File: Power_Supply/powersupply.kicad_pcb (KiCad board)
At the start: 2 copper layers, 60.8 x 63.3 mm, 80 parts, among them J1 1x2, J101 USB_B_Micro, J102 Conn_01x03_Male, J103 Default_Jumper, J104 Default_Jumper, J2 1x2, Q1 IRF9Z24NPBF, SW1 KMR2, SW2 joystick-K1-1506DN-01, U101 AZ1117E-3.3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

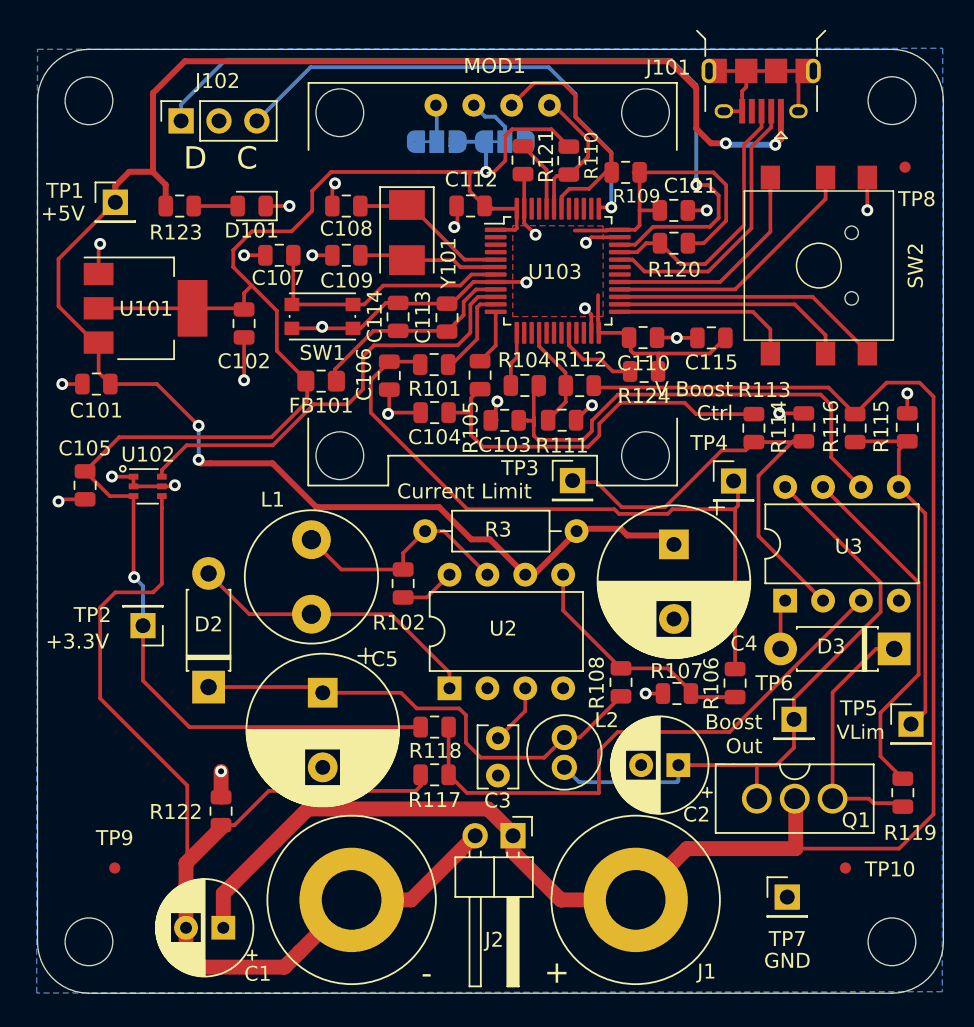
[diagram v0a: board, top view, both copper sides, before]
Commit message: Stuff for bootloader and MOSFET flat orientation
Moved power stuff to left and changed mosfet to flat orientation
Added LED for bootloader
Added button for entering bootloader mode
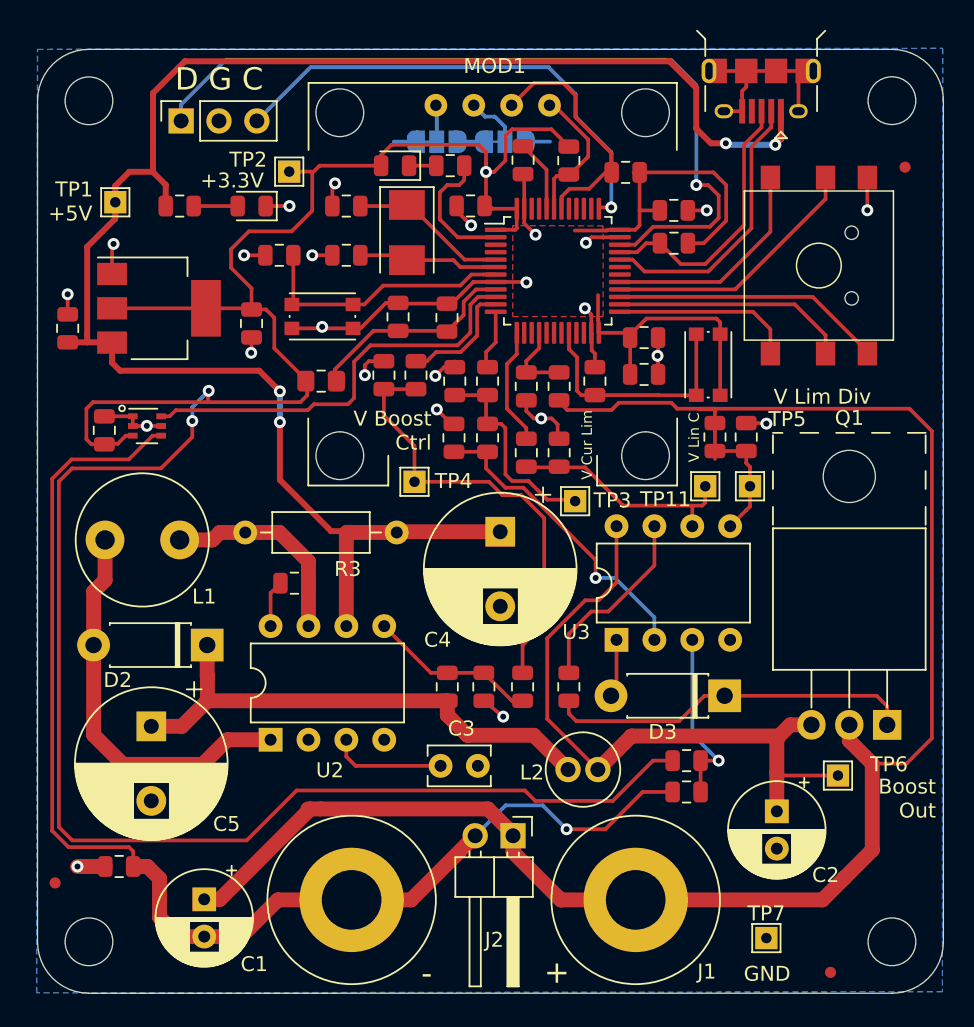
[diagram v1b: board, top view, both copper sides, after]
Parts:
- added D102: C503B 2.1V, LED_SMD:LED_0805_2012Metric, F.Cu at (52.8, 35.9)
- added G***: LOGO, powersupply:Logo, B.Cu at (60.1, 49.0)
- added R125: 4.99k, Resistor_SMD:R_0805_2012Metric, F.Cu at (56.5, 35.9)
- added SW3: KMR2, Button_Switch_SMD:SW_Push_1P1T_NO_CK_KMR2, F.Cu at (73.8, 49.2)
- added TP11: V_lin_ctrl, TestPoint:TestPoint_THTPad_1.5x1.5mm_Drill0.7mm, F.Cu at (73.6, 57.4)
- Q1: footprint powersupply:IRF9540N-PMOS -> Package_TO_SOT_THT:TO-220-3_Horizontal_TabUp
- R124: value 1.5k -> 4.99k
- TP1: value +5_isolated -> +5; footprint Connector_PinHeader_2.54mm:PinHeader_1x01_P2.54mm_Vertical -> TestPoint:TestPoint_THTPad_1.5x1.5mm_Drill0.7mm
- TP2, TP3, TP4, TP5, TP6, TP7: footprint Connector_PinHeader_2.54mm:PinHeader_1x01_P2.54mm_Vertical -> TestPoint:TestPoint_THTPad_1.5x1.5mm_Drill0.7mm
- moved TP2 32.0 mm to (45.7, 36.3)
- moved R119 23.5 mm to (64.5, 70.8)
- moved R114 23.5 mm to (56.8, 54.1)
- moved TP4 21.4 mm to (54.1, 57.1)
- moved TP5 19.3 mm to (76.6, 57.4)
- moved R113 17.9 mm to (59.0, 54.1)
- moved R118 17.0 mm to (72.3, 75.8)
- moved R117 16.9 mm to (72.3, 77.9)
- moved R106 14.3 mm to (61.4, 70.8)
- moved R107 13.0 mm to (58.8, 70.8), turned to 270 degrees
- moved U2 12.5 mm to (44.5, 74.4)
- moved R3 12.1 mm to (42.8, 60.5)
- moved D3 11.8 mm to (74.9, 71.5)
- moved C5 11.7 mm to (36.5, 73.5)
- moved C4 11.7 mm to (59.9, 60.5)
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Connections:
- R124 pad 1: +3V3 -> GND
- TP3 pad 1: /Current_limit_divider -> /V_curr_lim
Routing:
- net +3V3: track 153.4 -> 211.2 mm, vias 2 -> 3
- net Net-(R117-Pad1): track 38.6 -> 12.1 mm, vias 0 -> 1
- net /V_lin_ctrl: track 33.9 -> 15.6 mm
- net /V_boost_ctrl: track 46.3 -> 29.8 mm
- net /Voltage_limit_divider: track 23.7 -> 7.80 mm
- net /V_curr_lim: track 26.7 -> 13.8 mm
- net /Current_limit_divider: track 32.1 -> 20.9 mm, vias 0 -> 1
- net Net-(R119-Pad2): track 23.9 -> 12.9 mm
- net Net-(R124-Pad2): track 5.66 -> 16.3 mm
- net Net-(R125-Pad1): track 0.00 -> 8.99 mm
- net Net-(D3-Pad1): track 17.5 -> 24.7 mm
- net Net-(D2-Pad2): track 20.0 -> 26.8 mm
- net Net-(R106-Pad2): track 16.3 -> 11.4 mm
- net Net-(R104-Pad2): track 3.69 -> 7.91 mm
- net /V_positive_out: track 114.2 -> 118.2 mm
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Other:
- board text added: "D G C"
- board text added: "V Cur Lim"
- board text added: "V Lim Div"
- board text added: "V Lin C"
- board text removed: "Current Limit"
- board text removed: "D C"
- board text removed: "VLim"

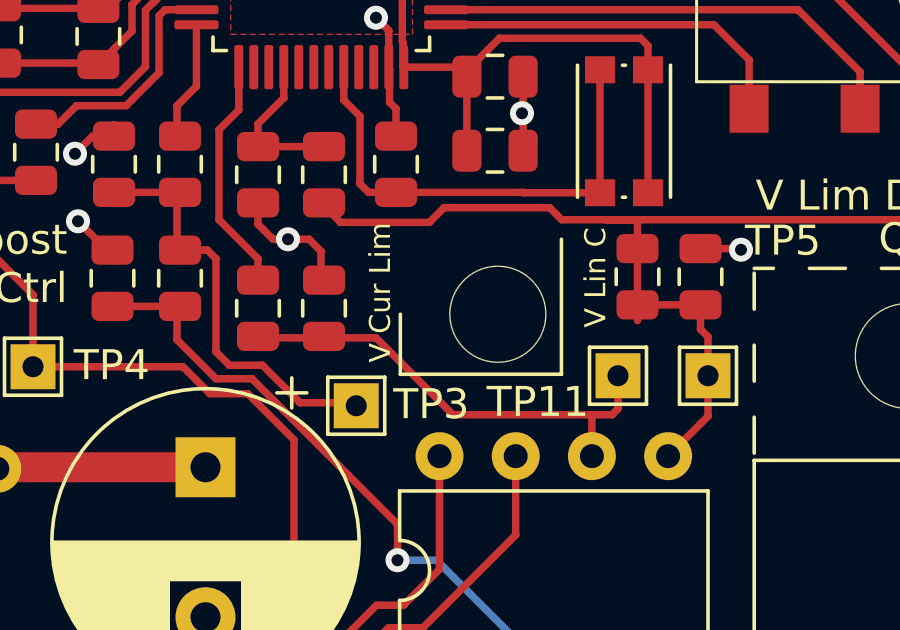
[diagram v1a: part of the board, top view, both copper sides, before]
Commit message: Ran DRC and fixed a rogue trace
Ran DRC
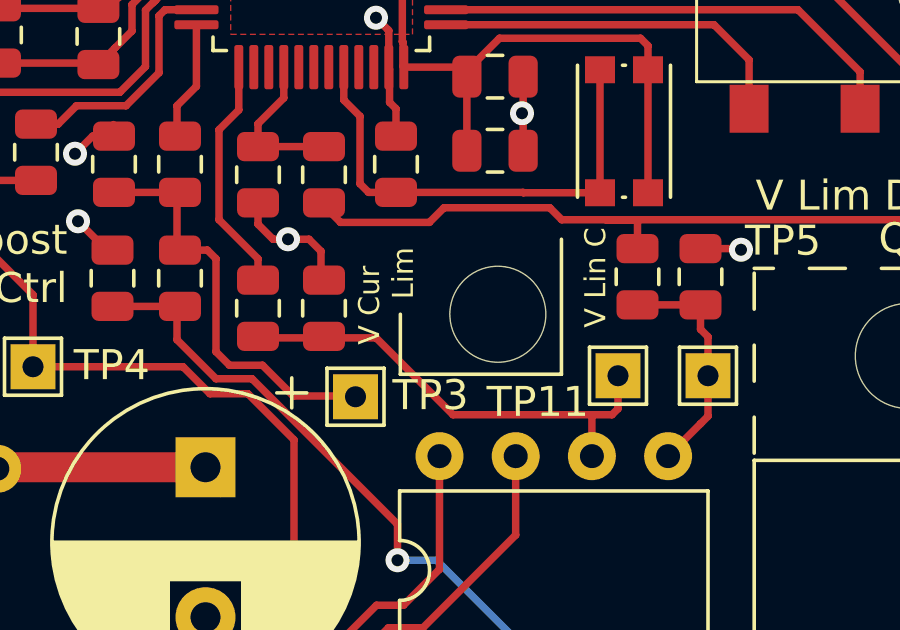
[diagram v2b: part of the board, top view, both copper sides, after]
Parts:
- moved TP3 0.30 mm to (64.8, 58.1)
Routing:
- net /V_positive_out: track 118.2 -> 115.8 mm
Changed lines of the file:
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@@
   )
   (module TestPoint:TestPoint_THTPad_1.5x1.5mm_Drill0.7mm (layer F.Cu)
-    (at 64.875 58.4)
+    (at 64.85 58.1)
     (descr "THT rectangular pad as test Point, square 1.5mm side length, hole diameter 0.7mm")
     (tags "test point THT pad rectangle square")
@@
   (gr_line (start 89.57 31.55) (end 89.57 87.95) (layer Edge.Cuts) (width 0.05))
   (gr_line (start 86.12 91.4) (end 32.25 91.4) (layer Edge.Cuts) (width 0.05))
-  (gr_text "V Cur Lim" (at 65.675 54.625 90) (layer F.SilkS)
+  (gr_text "V Cur\n       Lim" (at 65.875 55.05 90) (layer F.SilkS)
     (effects (font (size 0.7 0.7) (thickness 0.175)))
   )
@@
   (segment (start 56.8 51.2875) (end 58.9 51.2875) (width 0.25) (layer F.Cu) (net 6))
   (segment (start 58.9 51.2875) (end 58.9 53.2125) (width 0.25) (layer F.Cu) (net 6))
-  (segment (start 61.74999 57.04999) (end 63 58.3) (width 0.25) (layer F.Cu) (net 6))
   (segment (start 60.64999 57.04999) (end 61.74999 57.04999) (width 0.25) (layer F.Cu) (net 6))
   (segment (start 60.2 53.5) (end 60.2 56.6) (width 0.25) (layer F.Cu) (net 6))
-  (segment (start 63 58.3) (end 64.9 58.3) (width 0.25) (layer F.Cu) (net 6))
   (segment (start 59.9125 53.2125) (end 60.2 53.5) (width 0.25) (layer F.Cu) (net 6))
   (segment (start 60.2 56.6) (end 60.64999 57.04999) (width 0.25) (layer F.Cu) (net 6))
   (segment (start 59 53.2125) (end 59.9125 53.2125) (width 0.25) (layer F.Cu) (net 6))
+  (segment (start 62.775 58.075) (end 64.85 58.075) (width 0.25) (layer F.Cu) (net 6))
+  (segment (start 61.74999 57.04999) (end 62.775 58.075) (width 0.25) (layer F.Cu) (net 6))
   (segment (start 61.35 69.9125) (end 61.35 68.05) (width 0.25) (layer F.Cu) (net 7))
   (segment (start 61.35 68.05) (end 62.8 66.6) (width 0.25) (layer F.Cu) (net 7))
@@
   (segment (start 87.1 76) (end 88.8 74.3) (width 0.25) (layer F.Cu) (net 19))
   (segment (start 84.8 76) (end 87.1 76) (width 0.25) (layer F.Cu) (net 19))
-  (segment (start 74.25 52.25) (end 74.25 55.5625) (width 0.25) (layer F.Cu) (net 19))
-  (segment (start 74.3 52.2) (end 74.25 52.25) (width 0.25) (layer F.Cu) (net 19))
   (segment (start 73.2 52.2) (end 74.3 52.2) (width 0.25) (layer F.Cu) (net 19))
+  (segment (start 74.25 52.25) (end 74.25 53.1625) (width 0.25) (layer F.Cu) (net 19))
+  (segment (start 74.3 52.2) (end 74.25 52.25) (width 0.25) (layer F.Cu) (net 19))
   (via (at 66.25 63.55) (size 0.8) (drill 0.4) (layers F.Cu B.Cu) (net 20))
   (segment (start 67.55 63.55) (end 66.25 63.55) (width 0.25) (layer B.Cu) (net 20))

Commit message: Labelled buttons
Labelled buttons
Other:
- board text added: "BOOT1"
- board text added: "RESET"
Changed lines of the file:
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@@
   (general
     (thickness 1.6)
-    (drawings 21)
+    (drawings 23)
     (tracks 596)
     (zones 0)
@@
     (tags "test point THT pad rectangle square")
     (attr virtual)
-    (fp_text reference TP3 (at 2.5 -0.05) (layer F.SilkS)
+    (fp_text reference TP3 (at 2.475 0.2) (layer F.SilkS)
       (effects (font (size 1 1) (thickness 0.15)))
     )
@@
     )
   )
+  (gr_text BOOT1 (at 73.85 45.825) (layer F.SilkS)
+    (effects (font (size 0.8 0.8) (thickness 0.2)))
+  )
+  (gr_text RESET (at 48.025 43.725) (layer F.SilkS)
+    (effects (font (size 0.8 0.8) (thickness 0.2)))
+  )
   (gr_text "V Lim Div" (at 84.725 51.4) (layer F.SilkS)

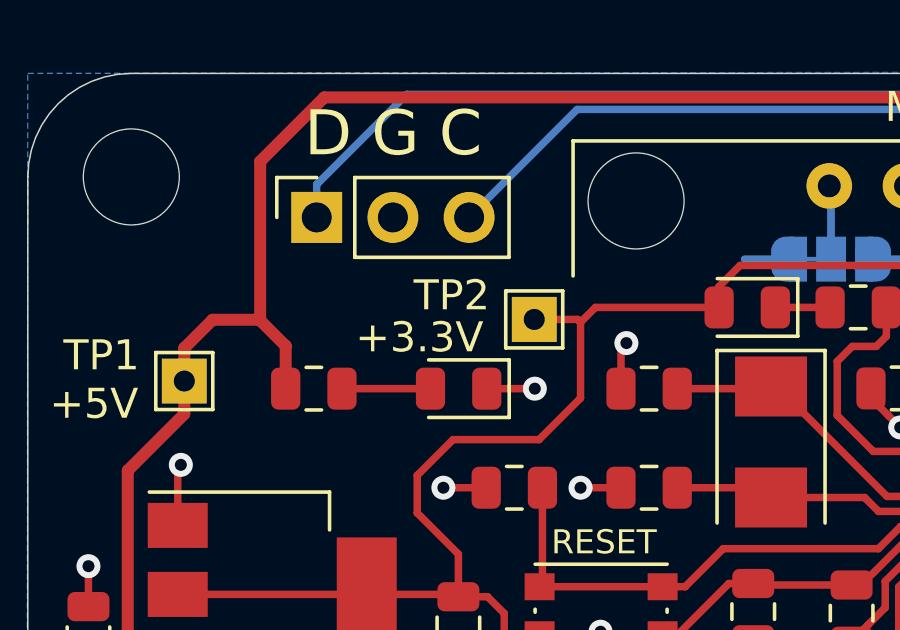
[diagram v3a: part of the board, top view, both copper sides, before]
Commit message: updated  net name for v_positive_out_div
updated  net name for v_positive_out_div
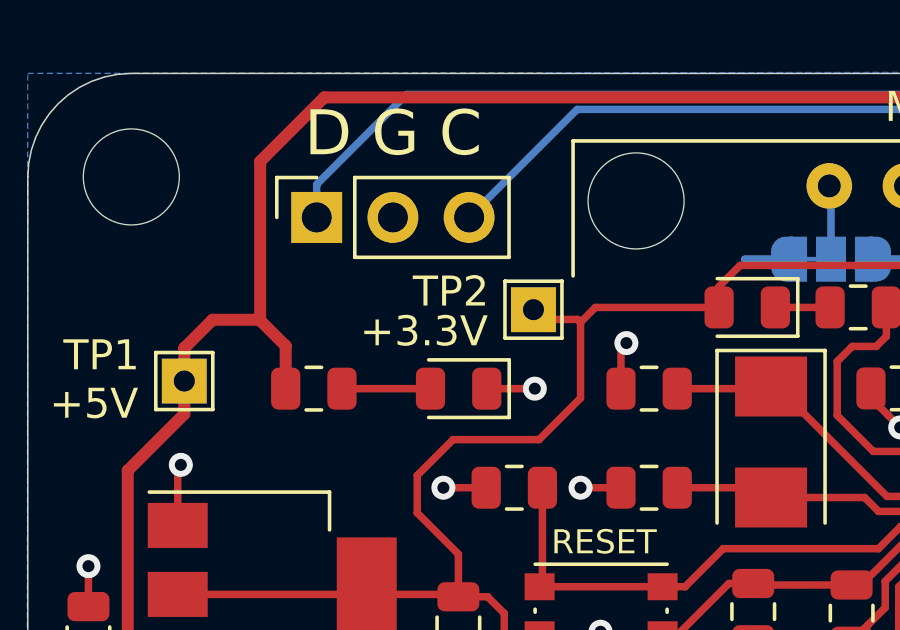
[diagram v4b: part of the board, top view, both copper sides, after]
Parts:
- moved TP2 0.33 mm to (45.7, 36.0)
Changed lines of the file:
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@@
     (visible_elements FFFDFF7F)
     (pcbplotparams
-      (layerselection 0x20000_7fffffff)
+      (layerselection 0x20000_7ffffffe)
       (usegerberextensions false)
       (usegerberattributes false)
       (usegerberadvancedattributes false)
       (creategerberjobfile false)
-      (excludeedgelayer false)
+      (excludeedgelayer true)
       (linewidth 0.100000)
       (plotframeref false)
@@
   )
   (module TestPoint:TestPoint_THTPad_1.5x1.5mm_Drill0.7mm (layer F.Cu)
-    (at 45.7 36.3 180)
+    (at 45.675 35.975 180)
     (descr "THT rectangular pad as test Point, square 1.5mm side length, hole diameter 0.7mm")
     (tags "test point THT pad rectangle square")
     (attr virtual)
-    (fp_text reference TP2 (at 2.75 0.8) (layer F.SilkS)
+    (fp_text reference TP2 (at 2.75 0.6) (layer F.SilkS)
       (effects (font (size 1 1) (thickness 0.15)))
     )
@@
     (effects (font (size 0.7 0.7) (thickness 0.175)))
   )
-  (gr_text +3.3V (at 41.875 36.9) (layer F.SilkS)
+  (gr_text +3.3V (at 42.025 36.7) (layer F.SilkS)
     (effects (font (size 1 1) (thickness 0.25)))
   )
